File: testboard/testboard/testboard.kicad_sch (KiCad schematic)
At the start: 13 parts, among them IC1 STGIPQ3H60T-HL, J1 Conn_01x02, J10 Conn_01x25, J11 Conn_01x25, J2 Conn_01x04, J3 Conn_01x08, J4 Conn_01x10, J5 Conn_01x02, J6 Conn_01x04, J7 STM32F407G-DISC1-SHIELD, J8 Conn_01x25, J9 Conn_01x25

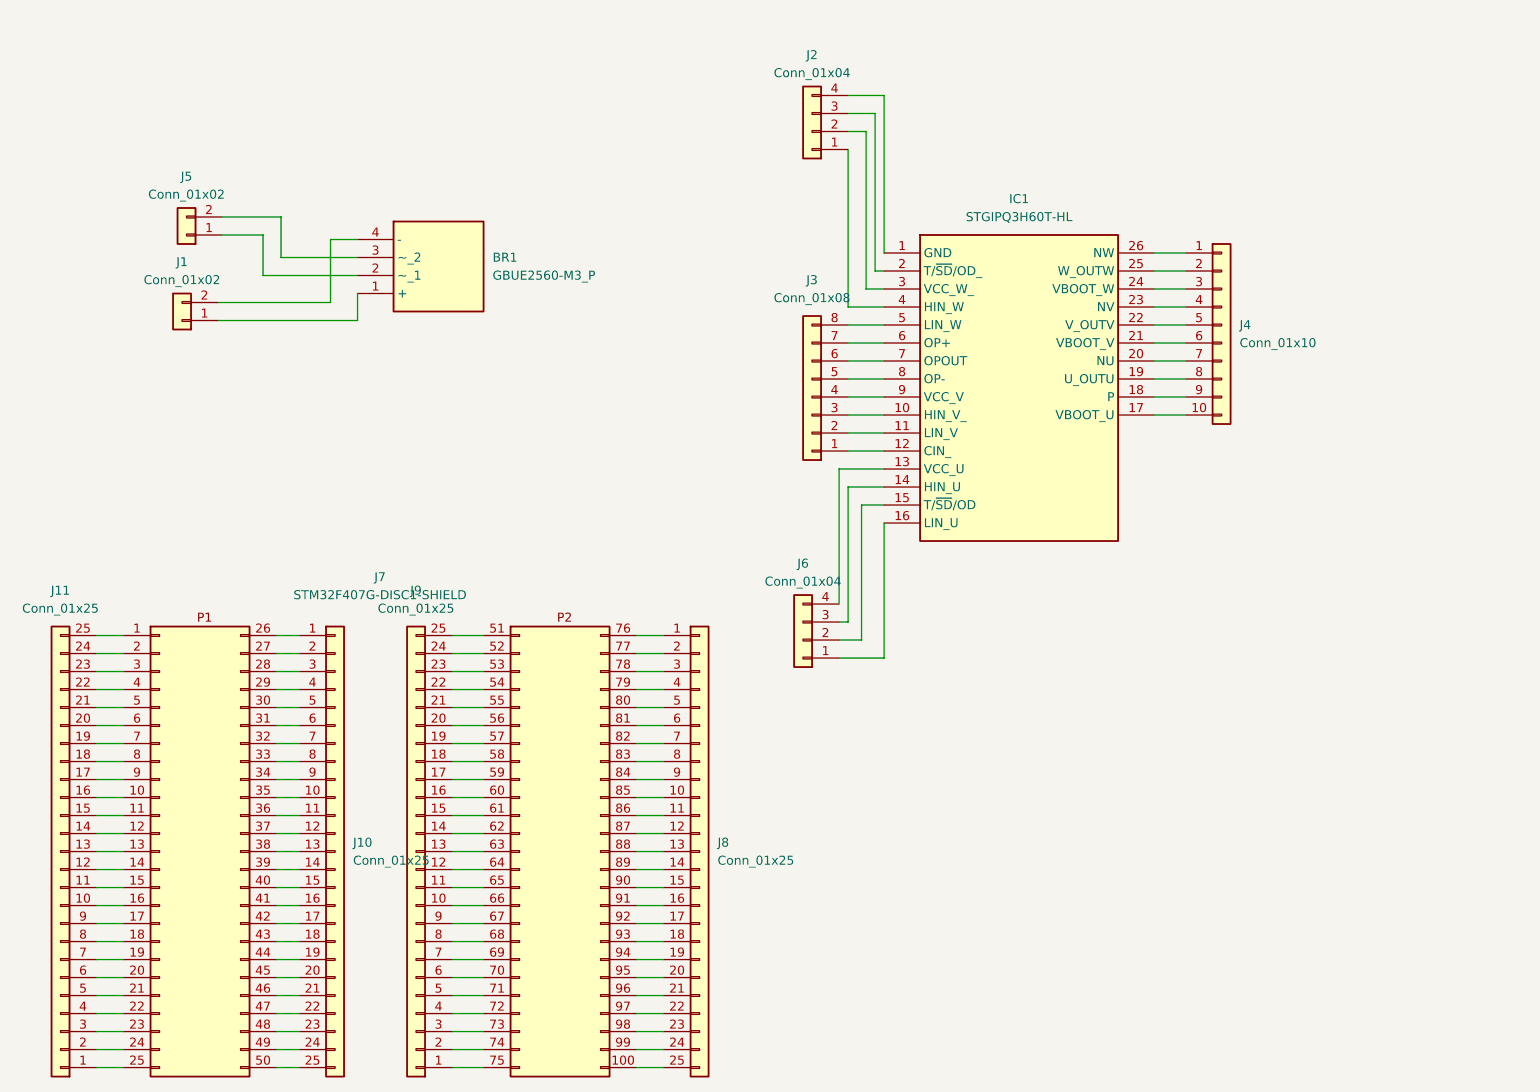
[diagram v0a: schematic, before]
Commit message: update schematics, BOM, & test board
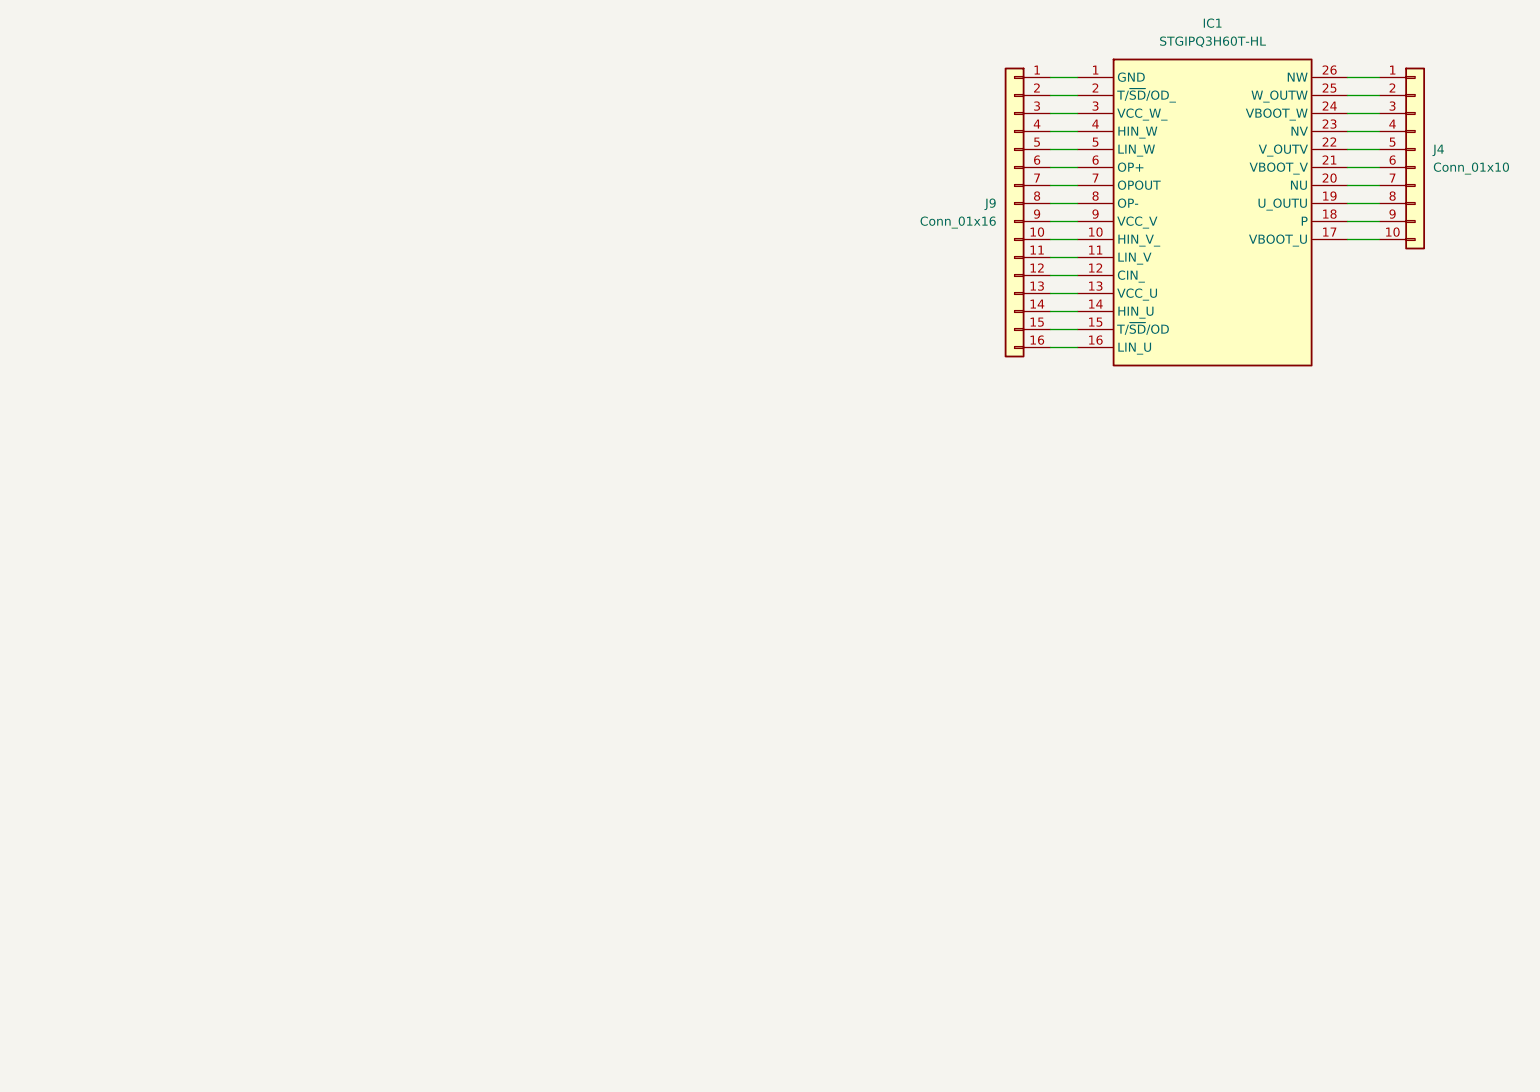
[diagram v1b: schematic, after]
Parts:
- removed BR1: GBUE2560-M3_P, SamacSys_Parts:GBUE2560M3P, symbol SamacSys_Parts:GBUE2560-M3_P
- removed J1, J5: Conn_01x02, Connector_Samtec_HPM_THT:Samtec_HPM-02-01-x-S_Straight_1x02_Pitch5.08mm, symbol Connector_Generic:Conn_01x02
- removed J10, J11, J8, J9: Conn_01x25, Connector_PinHeader_2.54mm:PinHeader_1x25_P2.54mm_Vertical, symbol Connector_Generic:Conn_01x25
- removed J2, J6: Conn_01x04, Connector_Samtec_HPM_THT:Samtec_HPM-04-01-x-S_Straight_1x04_Pitch5.08mm, symbol Connector_Generic:Conn_01x04
- removed J3: Conn_01x08, Connector_Samtec_HPM_THT:Samtec_HPM-08-01-x-S_Straight_1x08_Pitch5.08mm, symbol Connector_Generic:Conn_01x08
- removed J7: STM32F407G-DISC1-SHIELD, Custom:STM32F407G-DISC1-SHIELD, symbol Custom:STM32F407G-DISC1-SHIELD
- added J9: Conn_01x16, Connector_PinHeader_2.54mm:PinHeader_1x16_P2.54mm_Vertical, symbol Connector_Generic:Conn_01x16
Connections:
- net at IC1.4 (HIN_W): now also J9.4 (Pin_4)
- net at IC1.3 (VCC_W_): now also J9.3 (Pin_3)
- net at IC1.2 (T/~{SD}/OD_): now also J9.2 (Pin_2)
- net at IC1.1 (GND): now also J9.1 (Pin_1)
- net at IC1.10 (HIN_V_): now also J9.10 (Pin_10)
- net at IC1.11 (LIN_V): now also J9.11 (Pin_11)
- net at IC1.12 (CIN_): now also J9.12 (Pin_12)
- net at IC1.13 (VCC_U): now also J9.13 (Pin_13)
- net at IC1.14 (HIN_U): now also J9.14 (Pin_14)
- net at IC1.15 (T/~{SD}/OD): now also J9.15 (Pin_15)
- net at IC1.16 (LIN_U): now also J9.16 (Pin_16)
- net at IC1.5 (LIN_W): now also J9.5 (Pin_5)
- net at IC1.6 (OP+): now also J9.6 (Pin_6)
- net at IC1.7 (OPOUT): now also J9.7 (Pin_7)
- net at IC1.8 (OP-): now also J9.8 (Pin_8)
- net at IC1.9 (VCC_V): now also J9.9 (Pin_9)
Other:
- moved on the sheet: IC1, J4
